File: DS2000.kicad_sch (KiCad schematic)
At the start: 54 parts, among them J1 USB-C, J2 SWD, J3 USB wire, SW1 MUTE, SW2 DEAFEN, SW3 DISCONNECT, SW5 RESET, U1 USBLC6-2SC6, U2 AP2112K-3.3, U3 RP2350A, U4 W25Q32JVSS, U5 74AHCT1G125, Y1 12MHz

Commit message: feat: replace the RESET button with bridgeable pads
Like BOOTSEL, reset is a recovery tool rather than something used day to day: unplugging USB resets
the board, and firmware updates reboot into USB boot from software (DS-2000-Firmware#14, #15;
DS-2000#35). JP2 is an open solder jumper from RUN to GND, bridged briefly to reset; R9 keeps RUN
high. The visible face now has no tactile switches. ERC and the netlist check pass.
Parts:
- JP2: renamed from SW5; footprint Button_Switch_SMD:SW_Push_1P1T_XKB_TS-1187A -> Jumper:SolderJumper-2_P1.3mm_Open_RoundedPad1.0x1.5mm; symbol Switch:SW_Push -> Jumper:SolderJumper_2_Open; MPN TS-1187A-B-A-B -> (none); Manufacturer XKB -> (none); Note (none) -> Bridge briefly to reset; now left out of the parts list
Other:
- note added: "JP2: bridge briefly to reset. R9 keeps RUN high."
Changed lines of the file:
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@@
 		)
 	)
-	(text "Core regulator: layout exactly as the RP2350 guide"
+	(text "JP2: bridge briefly to reset. R9 keeps RUN high."
 		(exclude_from_sim no)
-		(at 148.59 121.92 0)
+		(at 241.3 86.36 0)
 		(effects
 			(font
@@
 		)
 	)
+	(text "C4 VREG_VIN · C6-C11 IOVDD x6 · C12-C14 DVDD x3 · C15 ADC_AVDD · C16 USB_OTP_VDD + QSPI_IOVDD (shared, as in the reference)"
+		(exclude_from_sim no)
+		(at 68.58 283.21 0)
+		(effects
+			(font
+				(size 1.27 1.27)
+				(italic yes)
+			)
+			(justify left bottom)
+		)
+	)
 	(text "12 MHz crystal, SWD"
 		(exclude_from_sim no)
@@
 		)
 	)
-	(text "D1 under mute, D2 under deafen (reverse-mounted). Disconnect key has no LED. One 100n per LED."
+	(text "GP0-GP2, internal pull-ups"
 		(exclude_from_sim no)
-		(at 214.63 227.33 0)
+		(at 227.33 149.86 0)
 		(effects
 			(font
@@
 		)
 	)
-	(text "C4 VREG_VIN · C6-C11 IOVDD x6 · C12-C14 DVDD x3 · C15 ADC_AVDD · C16 USB_OTP_VDD + QSPI_IOVDD (shared, as in the reference)"
+	(text "D1 under mute, D2 under deafen (reverse-mounted). Disconnect key has no LED. One 100n per LED."
 		(exclude_from_sim no)
-		(at 68.58 283.21 0)
+		(at 214.63 227.33 0)
 		(effects
 			(font
@@
 		)
 	)
-	(text "GP0-GP2, internal pull-ups"
+	(text "JP1: bridge the pads while plugging in USB to enter USB boot."
 		(exclude_from_sim no)
-		(at 227.33 149.86 0)
+		(at 68.58 170.18 0)
 		(effects
 			(font
@@
 		)
 	)
-	(text "JP1: bridge the pads while plugging in USB to enter USB boot."
+	(text "Core regulator: layout exactly as the RP2350 guide"
 		(exclude_from_sim no)
-		(at 68.58 170.18 0)
+		(at 148.59 121.92 0)
 		(effects
 			(font
@@
 	)
 	(symbol
-		(lib_id "Switch:SW_Push")
+		(lib_id "Jumper:SolderJumper_2_Open")
 		(at 264.16 60.96 270)
 		(unit 1)
 		(body_style 1)
 		(exclude_from_sim no)
-		(in_bom yes)
+		(in_bom no)
 		(on_board yes)
 		(in_pos_files yes)
 		(dnp no)
-		(property "Reference" "SW5"
+		(property "Reference" "JP2"
 			(at 267.97 60.96 0)
 			(show_name no)
@@
 			)
 		)
-		(property "Footprint" "Button_Switch_SMD:SW_Push_1P1T_XKB_TS-1187A"
+		(property "Footprint" "Jumper:SolderJumper-2_P1.3mm_Open_RoundedPad1.0x1.5mm"
 			(at 264.16 60.96 0)
 			(hide yes)
@@
 			)
 		)
-		(property "MPN" "TS-1187A-B-A-B"
-			(at 264.16 60.96 0)
-			(hide yes)
-			(show_name no)
-			(do_not_autoplace no)
-			(effects
-				(font
-					(size 1.27 1.27)
-				)
-			)
-		)
-		(property "Manufacturer" "XKB"
+		(property "Note" "Bridge briefly to reset"
 			(at 264.16 60.96 0)
 			(hide yes)
@@
 			(project ""
 				(path "/defea174-d404-5f0f-95d3-26e7103e2a73"
-					(reference "SW5")
+					(reference "JP2")
 					(unit 1)
 				)

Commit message: feat: start the rev A board with its mechanical layout fixed
tools/pcb-generator/gen_pcb.py builds the board from the schematic's netlist, so footprints, nets,
fields and symbol links match and DRC's schematic-parity check is clean. Update PCB from Schematic
reports no changes.

Fixed: a 72 x 50 mm outline with 3 mm corners, four M2 holes 4 mm in from the edges, the three keys
in a row at 19.05 mm, the two SK6812MINI-E under the mute and deafen switches' LED windows on the
bottom, and USB-C, SWD and the USB wire holes along the back edge. Everything else has a starting
position in the strip behind the keys, grouped around the RP2350A, and is meant to be moved.

Stackup is JLCPCB's JLC04161H-7628 (4 layers, 1.6 mm) with black mask and ENIG, In1 GND and In2
+3V3 planes and a GND pour on the bottom. Design rules follow JLC's minimums; the reverse-mount LED
cut-out gets its own 0.2 mm edge clearance in DS2000.kicad_dru. Net classes for power and USB.

The mounting holes are now excluded from the BOM in the schematic too, which is what the footprint
already said.

Remaining DRC output is routing (unconnected items, the +3V3 plane without vias yet) and footprint
silkscreen overlaps to tidy while laying out the face.
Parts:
- H1, H2, H3, H4: now left out of the parts list
- JP1: Note Bridge with tweezers while plugging in USB (or pressing RES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 -> Bridge with tweezers while plugging in USB (or while bridgi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
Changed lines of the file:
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@@
 		(body_style 1)
 		(exclude_from_sim no)
-		(in_bom yes)
+		(in_bom no)
 		(on_board yes)
 		(in_pos_files yes)
@@
 		(body_style 1)
 		(exclude_from_sim no)
-		(in_bom yes)
+		(in_bom no)
 		(on_board yes)
 		(in_pos_files yes)
@@
 		(body_style 1)
 		(exclude_from_sim no)
-		(in_bom yes)
+		(in_bom no)
 		(on_board yes)
 		(in_pos_files yes)
@@
 			)
 		)
-		(property "Note" "Bridge with tweezers while plugging in USB (or pressing RESET) to enter USB boot"
+		(property "Note" "Bridge with tweezers while plugging in USB (or while bridging JP2) to enter USB boot"
 			(at 114.3 177.8 0)
 			(hide yes)
@@
 		(body_style 1)
 		(exclude_from_sim no)
-		(in_bom yes)
+		(in_bom no)
 		(on_board yes)
 		(in_pos_files yes)

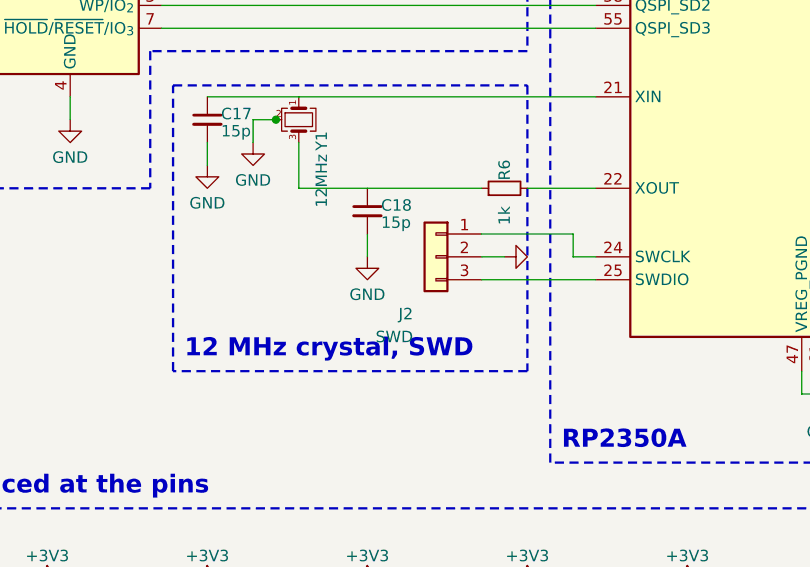
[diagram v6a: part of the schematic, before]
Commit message: feat: route rev A, shrink the board and move debug underneath
The board is now fully routed: DRC reports no unconnected pads, no clearance or edge errors and
full schematic parity. Only footprint silkscreen overlaps remain.

- 72 x 46 mm, 4 mm shallower: with the USB-C underneath and the SWD connector gone, the strip
  behind the keys needed less depth
- USB-C face now 1.2 mm past the back edge; its front shield tabs keep 0.6 mm of board
- SWD is three bare pads instead of the JST connector, and every debug pad (SWD, BOOT, RST) sits on
  the bottom with its own label
- top-side parts rearranged around the RP2350A pins they serve; decoupling caps in line with their
  pins, USB series resistors between the USB-C pegs straight above D+/D-
- LEDs turned so the data chain runs straight from D1 to D2; bottom GND pour joins pads solidly

Routing is reproducible with tools/pcb-generator/pipeline.py: plane fanout for GND and +3V3 (RP2350A
supply pins tied straight to their capacitors, pins 53/54 sharing one via), then Freerouting for
everything else, with incremental passes. The pipeline writes to build/ and never touches the
committed board, which is now edited by hand.

The core regulator still needs comparing with Raspberry Pi's reference layout before ordering; the
design notes list that and the other checks.
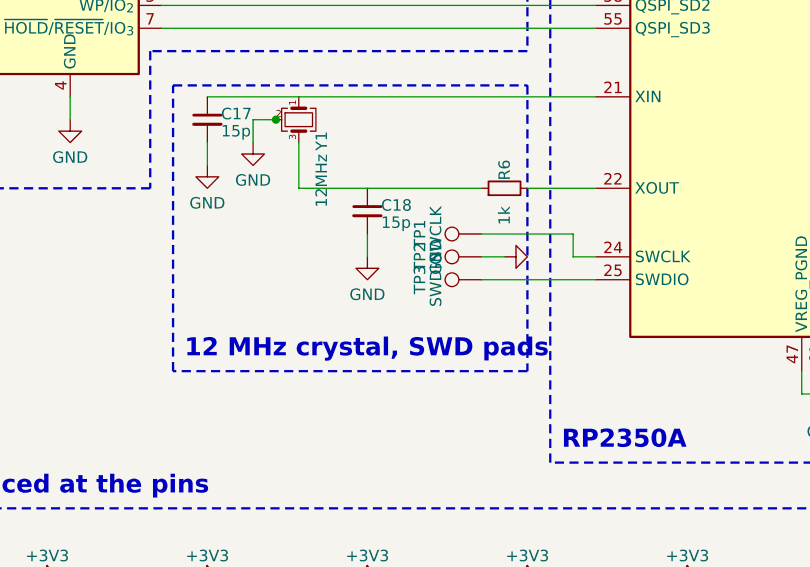
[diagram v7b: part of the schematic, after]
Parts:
- added SW1: MUTE, Button_Switch_Keyboard:SW_Cherry_MX_1.00u_PCB, symbol Switch:SW_Push
- added TP2: GND, TestPoint:TestPoint_Pad_D1.5mm, symbol Connector:TestPoint
- TP1: renamed from J2; value SWD -> SWCLK; footprint Connector_JST:JST_SH_SM03B-SRSS-TB_1x03-1MP_P1.00mm_Horizontal -> TestPoint:TestPoint_Pad_D1.5mm; symbol Connector_Generic:Conn_01x03 -> Connector:TestPoint; MPN SM03B-SRSS-TB -> (none); Manufacturer JST -> (none); Note Raspberry Pi Debug Probe pinout -> SWD pad, bottom side; now left out of the parts list
- TP3: renamed from SW1; value MUTE -> SWDIO; footprint Button_Switch_Keyboard:SW_Cherry_MX_1.00u_PCB -> TestPoint:TestPoint_Pad_D1.5mm; symbol Switch:SW_Push -> Connector:TestPoint; Note (none) -> SWD pad, bottom side; now left out of the parts list
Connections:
- net GND: now also SW1.2, TP2.1; no longer TP1.2 (Pin_2), TP3.2
- net at U3.2 (GPIO0): now also SW1.1; no longer TP3.1
- net at U3.25 (SWDIO): now also TP3.1; no longer TP1.3 (Pin_3)
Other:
- note added: "12 MHz crystal, SWD pads"
- note removed: "12 MHz crystal, SWD"
